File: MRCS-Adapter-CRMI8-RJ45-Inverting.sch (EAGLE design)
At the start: 17 parts, among them CON1 CONNECTOR-M033.5MM-LOCK, J1 RJ45, M1 MOUNTINGHOLE, M2 MOUNTINGHOLE

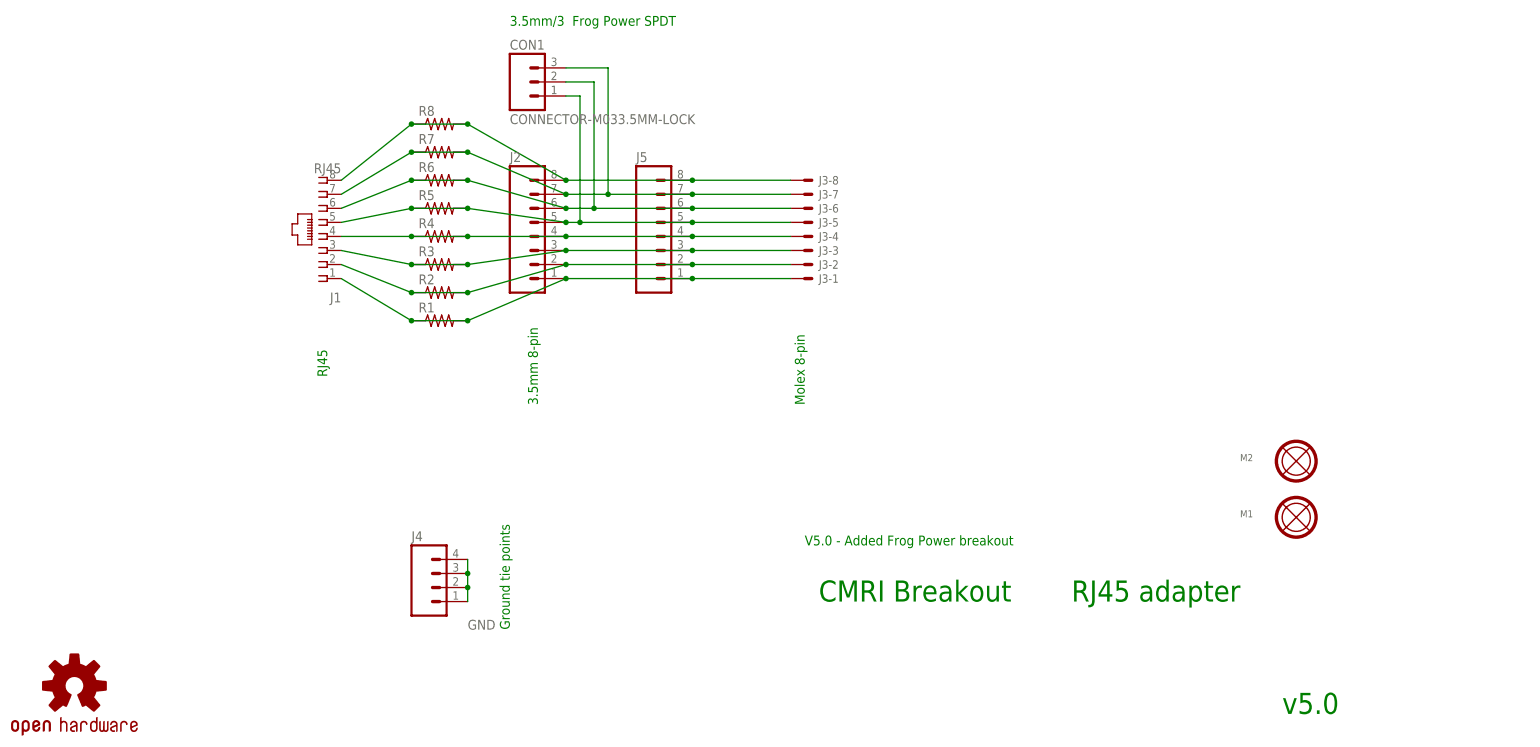
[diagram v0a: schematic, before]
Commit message: added 74LS540, modified connectors
Added inverter (74LS540), removed frog connector, added Vcc, Gnd for logic supply
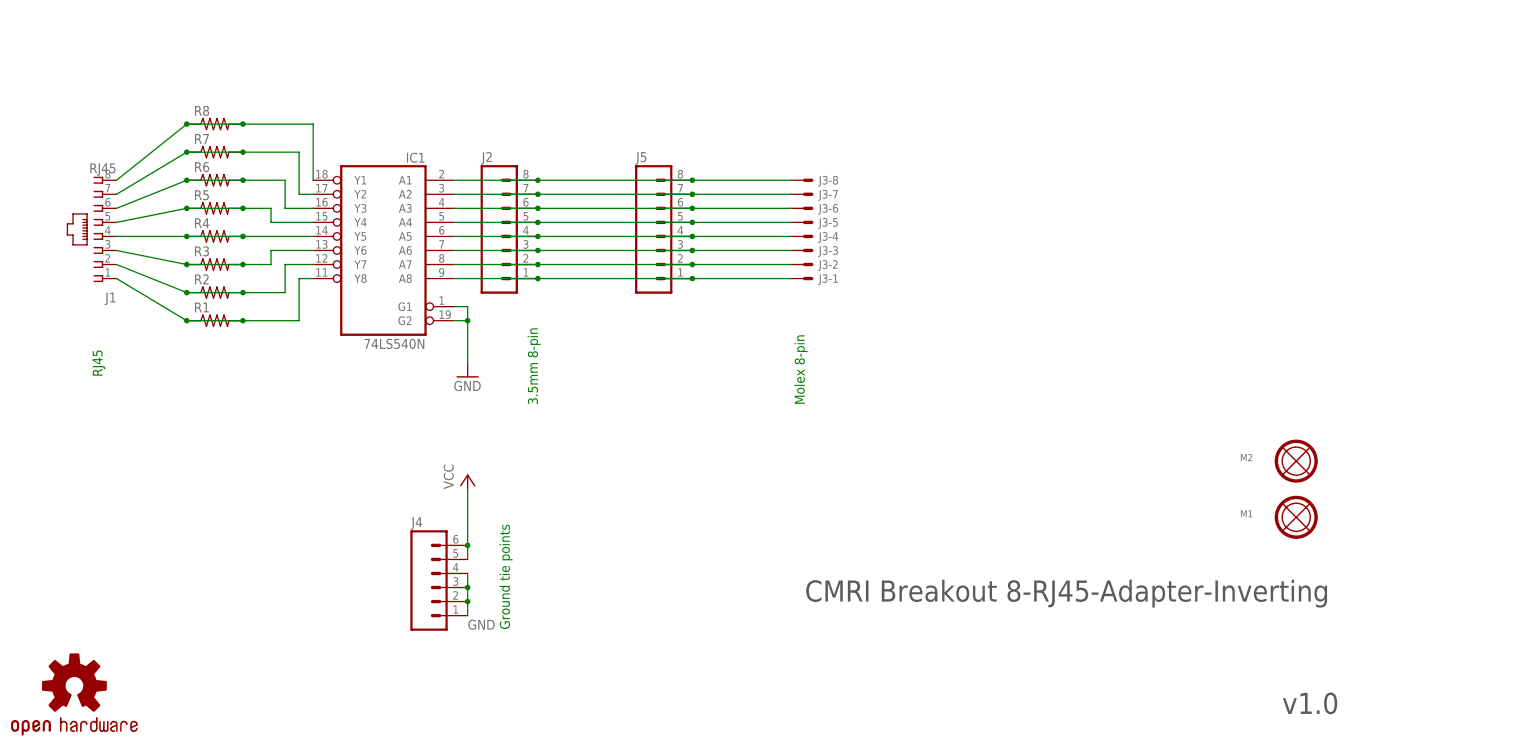
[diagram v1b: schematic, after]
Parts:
- removed CON1: CONNECTOR-M033.5MM-LOCK, SPCoast:CONNECTOR-M033.5MM-LOCK
- added IC1: 74LS540N, 74xx-us:74LS540N
- J4: device SPCoast:CONNECTOR-M04SCREW_LOCK -> SPCoast:CONNECTOR-M06LOCK
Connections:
- new net N$2: IC1A.Y1, J1.8, R8.1, R8.2
- new net N$3: IC1A.Y2, J1.7, R7.1, R7.2
- new net N$4: IC1A.Y3, J1.6, R6.1, R6.2
- new net N$5: IC1A.Y4, J1.5, R5.1, R5.2
- new net N$6: IC1A.Y5, J1.4, R4.1, R4.2
- new net N$7: IC1A.Y6, J1.3, R3.1, R3.2
- new net N$8: IC1A.Y7, J1.2, R2.1, R2.2
- new net N$9: IC1A.Y8, J1.1, R1.1, R1.2
- new net VCC: J4.5, J4.6
- net GND: now also IC1A.G1, IC1A.G2
- net L1: now also IC1A.A8; no longer J1.1, R1.1, R1.2
- net L2: now also IC1A.A7; no longer J1.2, R2.1, R2.2
- net L3: now also IC1A.A6; no longer J1.3, R3.1, R3.2
- net L4: now also IC1A.A5; no longer J1.4, R4.1, R4.2
- net L5: now also IC1A.A4; no longer CON1.1, J1.5, R5.1, R5.2
- net L6: now also IC1A.A3; no longer CON1.2, J1.6, R6.1, R6.2
- net L7: now also IC1A.A2; no longer CON1.3, J1.7, R7.1, R7.2
- net L8: now also IC1A.A1; no longer J1.8, R8.1, R8.2
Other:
- note added: "CMRI Breakout 8-RJ45-Adapter-Inverting"
- note added: "v1.0"
- note removed: "3.5mm/3 Frog Power SPDT"
- note removed: "CMRI Breakout"
- note removed: "RJ45 adapter"
- note removed: "V5.0 - Added Frog Power breakout"
- note removed: "v5.0"
- moved on the sheet: J1, J2, R1, R2, R3, R4, R5, R6, R7, R8

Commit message: various adjustments
minor board layout adjustments
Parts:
- added RN1: 4.7K, resistor-sil:GE08RP
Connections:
- net L1: now also RN1H.2
- net L2: now also RN1G.2
- net L3: now also RN1F.2
- net L4: now also RN1E.2
- net L5: now also RN1D.2
- net L6: now also RN1C.2
- net L7: now also RN1B.2
- net L8: now also RN1A.2
- net VCC: now also RN1A.1
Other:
- moved on the sheet: J2, J3-1, J3-2, J3-3, J3-4, J3-5, J3-6, J3-7, J3-8, J5

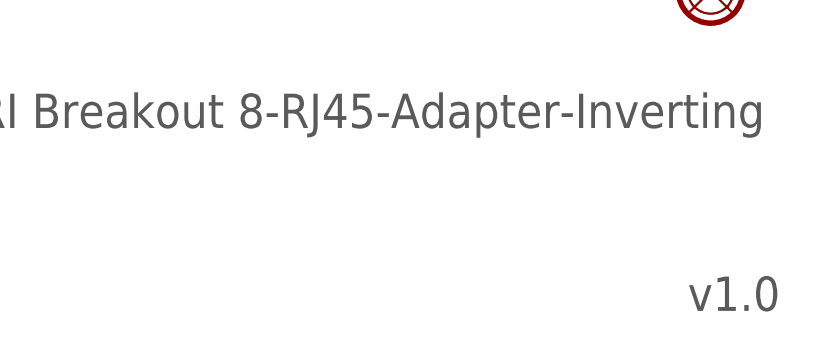
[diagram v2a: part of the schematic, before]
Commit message: final changes for panelizing
clean up to facilitate the panelizer
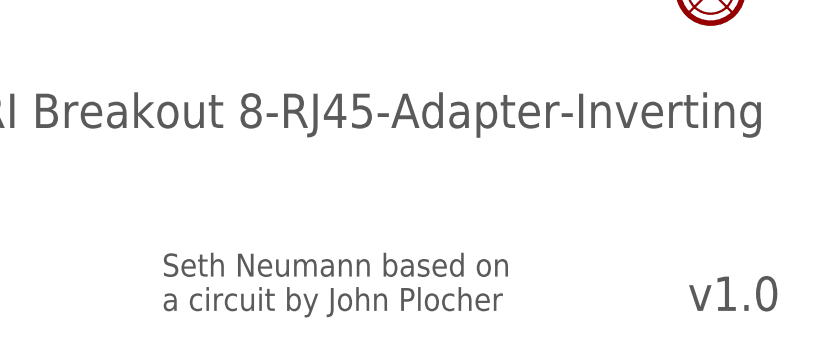
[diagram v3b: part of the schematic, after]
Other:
- note added: "Seth Neumann based on a circuit by John Plocher"
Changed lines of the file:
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@@
 <text x="96.52" y="22.86" size="1.778" layer="91" rot="R90">Ground tie points</text>
 <text x="149.86" y="27.94" size="3.81" layer="97">CMRI Breakout 8-RJ45-Adapter-Inverting</text>
+<text x="177.8" y="7.62" size="2.54" layer="97" font="vector">Seth Neumann based on
+a circuit by John Plocher</text>
 </plain>
 <instances>

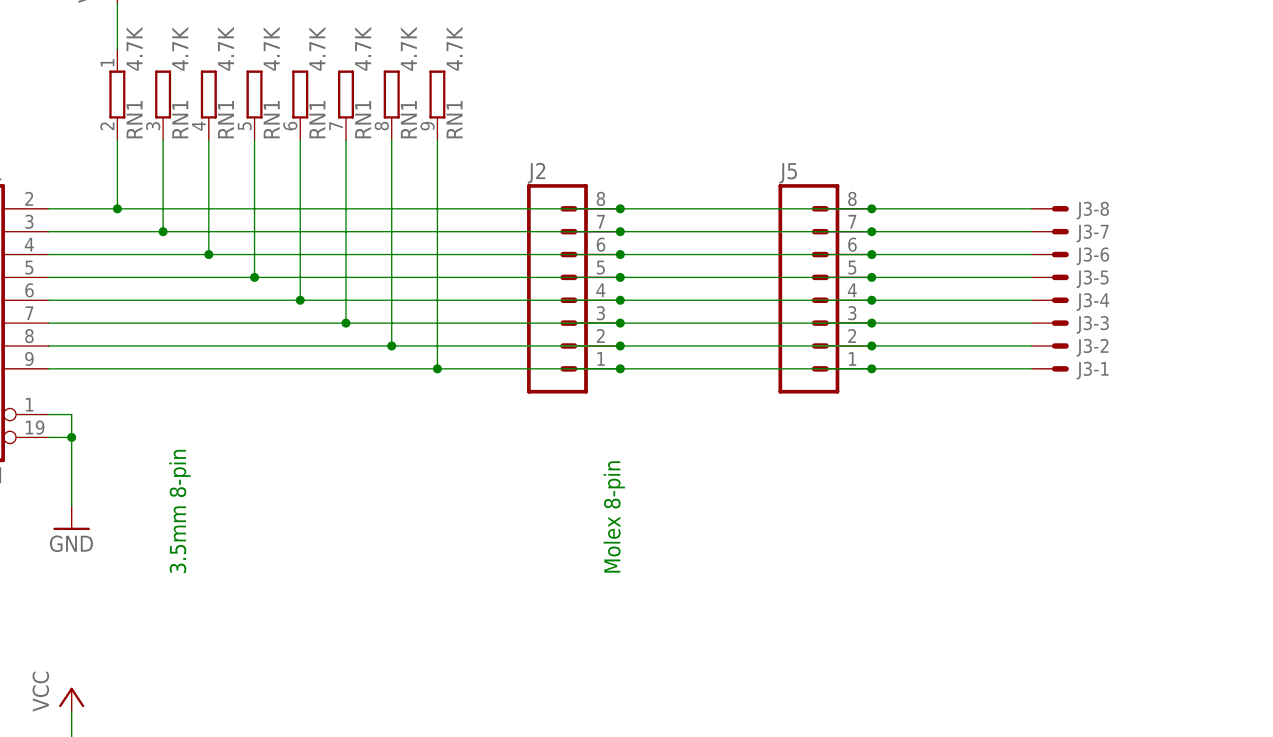
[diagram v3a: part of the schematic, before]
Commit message: label changes for legibility
label changes for legibility
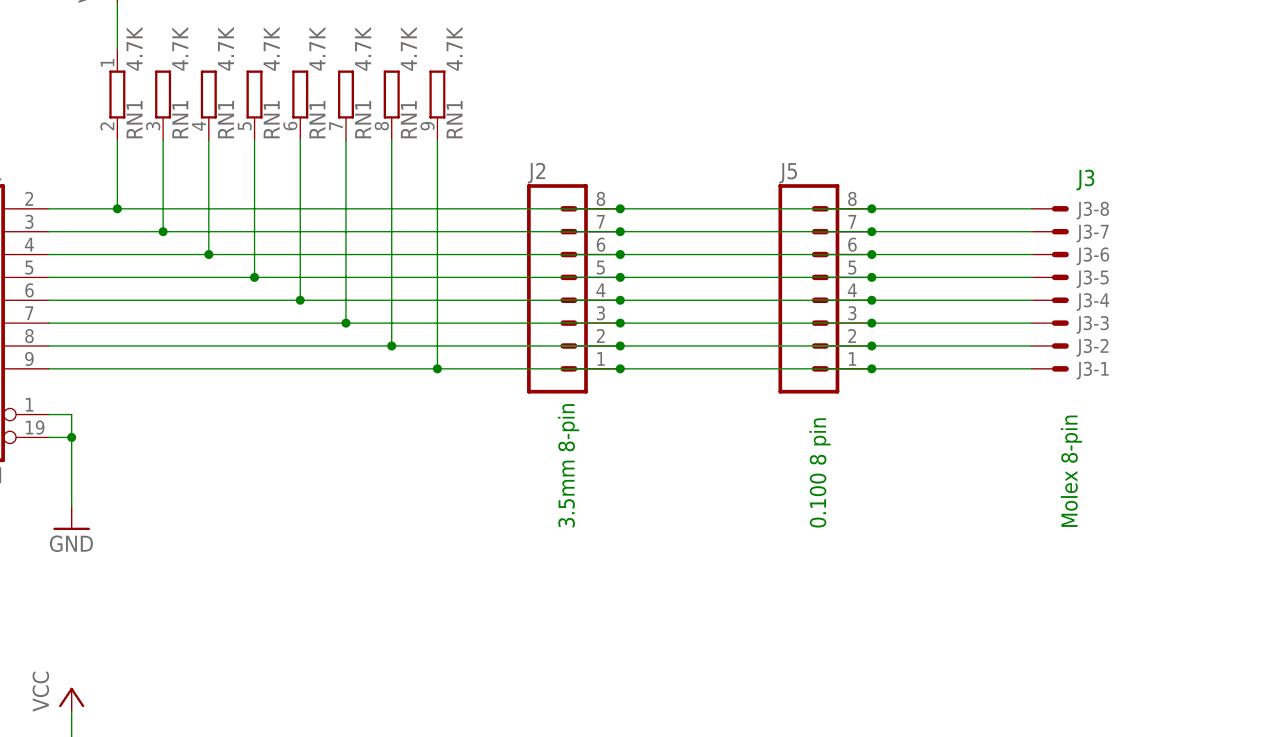
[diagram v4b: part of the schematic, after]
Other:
- note added: "0.100 8 pin"
- note added: "J3"
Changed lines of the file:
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@@
 <sheet>
 <plain>
-<text x="149.86" y="63.5" size="1.778" layer="91" rot="R90">Molex 8-pin</text>
-<text x="101.6" y="63.5" size="1.778" layer="91" rot="R90">3.5mm 8-pin</text>
+<text x="200.66" y="68.58" size="1.778" layer="91" rot="R90">Molex 8-pin</text>
+<text x="144.78" y="68.58" size="1.778" layer="91" rot="R90">3.5mm 8-pin</text>
 <text x="22.86" y="68.58" size="1.778" layer="91" rot="R90">RJ45</text>
 <text x="236.22" y="7.62" size="3.81" layer="97">v1.0</text>
@@
 <text x="177.8" y="7.62" size="2.54" layer="97" font="vector">Seth Neumann based on
 a circuit by John Plocher</text>
+<text x="172.72" y="68.58" size="1.778" layer="91" rot="R90">0.100 8 pin</text>
+<text x="200.66" y="106.68" size="1.778" layer="91">J3</text>
 </plain>
 <instances>
 <instance part="FRAME1" gate="G$1" x="0" y="0"/>
 <instance part="FRAME1" gate="G$2" x="147.32" y="0"/>
-<instance part="J3" gate="-1" x="198.12" y="86.36" rot="MR180"/>
+<instance part="J3" gate="-1" x="198.12" y="86.36" smashed="yes" rot="MR180">
+<attribute name="NAME" x="200.66" y="87.122" size="1.524" layer="95" rot="MR180"/>
+<attribute name="VALUE" x="197.358" y="84.963" size="1.778" layer="96" rot="MR180"/>
+</instance>
 <instance part="J3" gate="-2" x="198.12" y="88.9" rot="MR180"/>
 <instance part="J3" gate="-3" x="198.12" y="91.44" rot="MR180"/>
